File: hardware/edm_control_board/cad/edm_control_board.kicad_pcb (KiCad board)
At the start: 4 copper layers, 240 x 100 mm, 62 parts, among them J401 Conn_02x08_Odd_Even, J402 Conn_01x02, J403 Conn_01x02, J404 Conn_01x02, J405 Conn_01x06, Q201 BSS214NW, Q202 BSS214NW, Q203 BSS214NW, Q204 BSS214NW, SW501 SW_Push, SW502 SW_Push, SW503 SW_Push, SW504 SW_Push, U301 STM32F722RETx, U302 R-78E3.3-1.0, U303 L78L05_SO8, U501 NHD-0420H1Z, Y201 25M

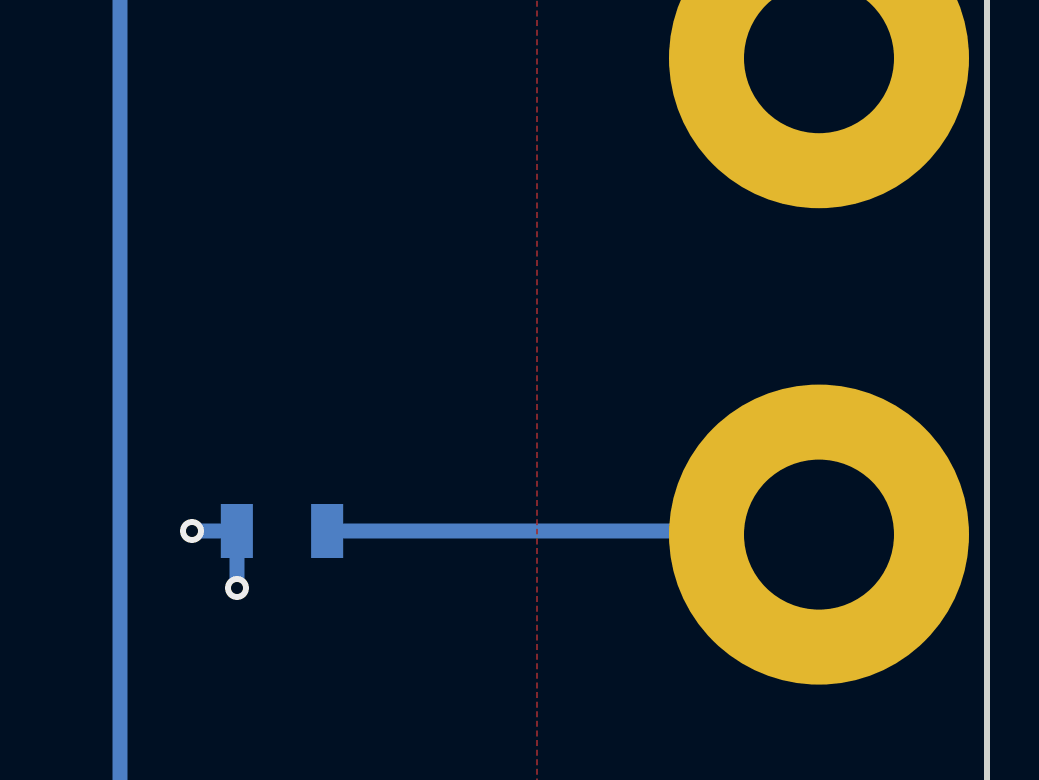
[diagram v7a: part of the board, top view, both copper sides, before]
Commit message: Add Y capacitor
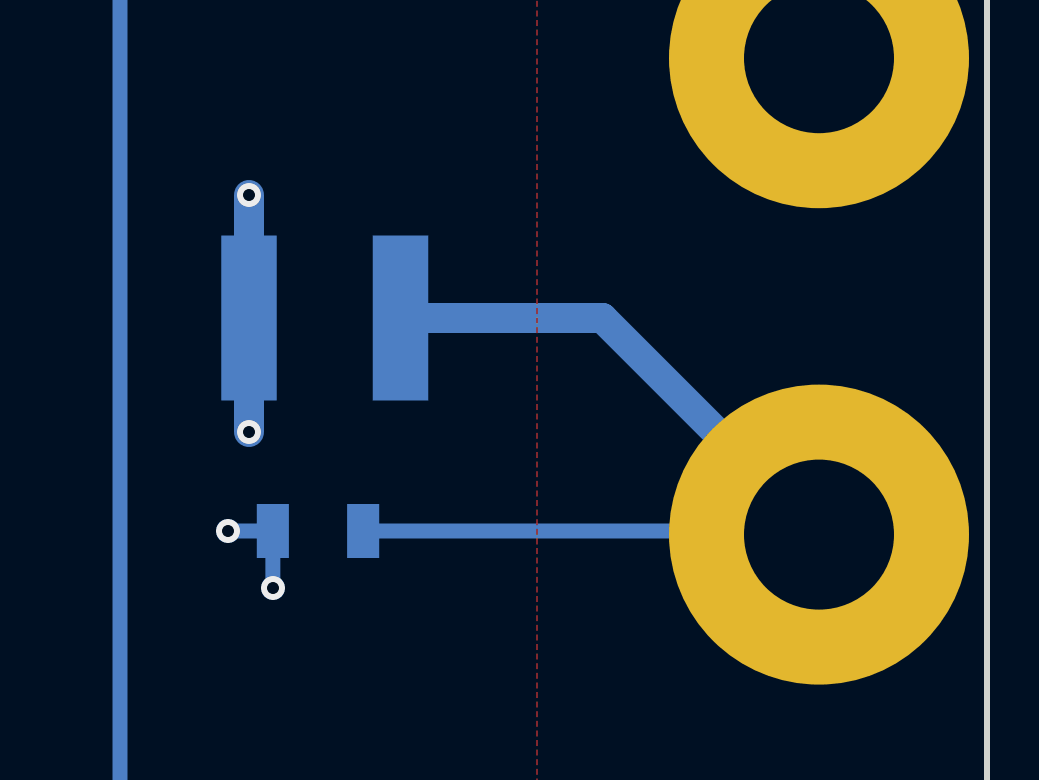
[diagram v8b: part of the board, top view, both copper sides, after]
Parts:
- added C401: 1800p, Capacitor_SMD:C_2220_5650Metric, B.Cu at (217.9, -33.4)
- moved R401 1.20 mm to (217.7, -26.3)
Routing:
- net /Connectors/Shield: track 16.4 -> 33.4 mm
- net GND: track 97.9 -> 105.8 mm, vias 27 -> 29
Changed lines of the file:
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@@
     (thickness 1.6)
     (drawings 34)
-    (tracks 490)
+    (tracks 496)
     (zones 0)
-    (modules 62)
+    (modules 63)
     (nets 68)
   )
@@
   )
   (setup
-    (last_trace_width 0.5)
+    (last_trace_width 1)
     (user_trace_width 0.25)
     (user_trace_width 0.5)
@@
     (uvia_drill 0.1)
   )
+  (module Capacitor_SMD:C_2220_5650Metric (layer B.Cu)
+    (at 217.925 -33.4 180)
+    (descr "Capacitor SMD 2220 (5650 Metric), square (rectangular) end terminal, IPC_7351 nominal, (Body size from: http://datasheets.avx.com/AVX-HV_MLCC.pdf), generated with kicad-footprint-generator")
+    (tags capacitor)
+    (attr smd)
+    (fp_text reference C401 (at 0 3.75 180) (layer B.SilkS)
+      (effects (font (size 1 1) (thickness 0.15)) (justify mirror))
+    )
+    (fp_text value 1800p (at 0 -3.75 180) (layer B.Fab)
+      (effects (font (size 1 1) (thickness 0.15)) (justify mirror))
+    )
+    (fp_line (start -2.85 -2.5) (end -2.85 2.5) (layer B.Fab) (width 0.1))
+    (fp_line (start -2.85 2.5) (end 2.85 2.5) (layer B.Fab) (width 0.1))
+    (fp_line (start 2.85 2.5) (end 2.85 -2.5) (layer B.Fab) (width 0.1))
+    (fp_line (start 2.85 -2.5) (end -2.85 -2.5) (layer B.Fab) (width 0.1))
+    (fp_line (start -1.28 2.61) (end 1.28 2.61) (layer B.SilkS) (width 0.12))
+    (fp_line (start -1.28 -2.61) (end 1.28 -2.61) (layer B.SilkS) (width 0.12))
+    (fp_line (start -3.7 -3) (end -3.7 3) (layer B.CrtYd) (width 0.05))
+    (fp_line (start -3.7 3) (end 3.7 3) (layer B.CrtYd) (width 0.05))
+    (fp_line (start 3.7 3) (end 3.7 -3) (layer B.CrtYd) (width 0.05))
+    (fp_line (start 3.7 -3) (end -3.7 -3) (layer B.CrtYd) (width 0.05))
+    (fp_text user %R (at 0 0 180) (layer B.Fab)
+      (effects (font (size 1 1) (thickness 0.15)) (justify mirror))
+    )
+    (pad 1 smd rect (at -2.525 0 180) (size 1.85 5.5) (layers B.Cu B.Paste B.Mask)
+      (net 63 /Connectors/Shield))
+    (pad 2 smd rect (at 2.525 0 180) (size 1.85 5.5) (layers B.Cu B.Paste B.Mask)
+      (net 12 GND))
+    (model ${KISYS3DMOD}/Capacitor_SMD.3dshapes/C_2220_5650Metric.wrl
+      (at (xyz 0 0 0))
+      (scale (xyz 1 1 1))
+      (rotate (xyz 0 0 0))
+    )
+  )
   (module Connector_PinHeader_2.54mm:PinHeader_2x08_P2.54mm_Vertical (layer B.Cu)
     (at 203 -39)
@@
   )
   (module Resistor_SMD:R_1206_3216Metric (layer B.Cu)
-    (at 216.5 -26.3 180)
+    (at 217.7 -26.3 180)
     (descr "Resistor SMD 1206 (3216 Metric), square (rectangular) end terminal, IPC_7351 nominal, (Body size source: http://www.tortai-tech.com/upload/download/2011102023233369053.pdf), generated with kicad-footprint-generator")
     (tags resistor)
@@
   (segment (start 165.5 -30) (end 165.5 -26.2) (width 0.5) (layer B.Cu) (net 11))
   (segment (start 179.38 -6.3) (end 182.08 -9) (width 0.5) (layer B.Cu) (net 11))
-  (segment (start 214.995 -26.3) (end 213.5 -26.3) (width 0.5) (layer B.Cu) (net 12))
-  (via (at 213.5 -26.3) (size 0.8) (drill 0.4) (layers F.Cu B.Cu) (net 12))
-  (segment (start 214.995 -24.405) (end 215 -24.4) (width 0.5) (layer B.Cu) (net 12))
-  (segment (start 214.995 -26.3) (end 214.995 -24.405) (width 0.5) (layer B.Cu) (net 12))
-  (via (at 215 -24.4) (size 0.8) (drill 0.4) (layers F.Cu B.Cu) (net 12))
+  (segment (start 215.4 -33.4) (end 215.4 -29.6) (width 1) (layer B.Cu) (net 12))
+  (via (at 215.4 -29.6) (size 0.8) (drill 0.4) (layers F.Cu B.Cu) (net 12))
+  (segment (start 215.4 -33.4) (end 215.4 -37.5) (width 1) (layer B.Cu) (net 12))
+  (via (at 215.4 -37.5) (size 0.8) (drill 0.4) (layers F.Cu B.Cu) (net 12))
+  (segment (start 216.195 -26.3) (end 214.7 -26.3) (width 0.5) (layer B.Cu) (net 12))
+  (via (at 214.7 -26.3) (size 0.8) (drill 0.4) (layers F.Cu B.Cu) (net 12))
+  (segment (start 216.195 -24.405) (end 216.2 -24.4) (width 0.5) (layer B.Cu) (net 12))
+  (segment (start 216.195 -26.3) (end 216.195 -24.405) (width 0.5) (layer B.Cu) (net 12))
+  (via (at 216.2 -24.4) (size 0.8) (drill 0.4) (layers F.Cu B.Cu) (net 12))
   (segment (start 201.6 -9) (end 197.6 -9) (width 2) (layer B.Cu) (net 12))
   (segment (start 206 -9) (end 201.6 -9) (width 2) (layer B.Cu) (net 12))
@@
   (segment (start 44.1 -22.6) (end 45.54999 -24.04999) (width 0.25) (layer B.Cu) (net 62))
   (segment (start 45.54999 -24.04999) (end 78.05001 -24.04999) (width 0.25) (layer B.Cu) (net 62))
-  (segment (start 218.005 -26.3) (end 234.28 -26.3) (width 0.5) (layer B.Cu) (net 63))
+  (segment (start 220.45 -33.4) (end 227.18 -33.4) (width 1) (layer B.Cu) (net 63))
+  (segment (start 227.18 -33.4) (end 234.4 -26.18) (width 1) (layer B.Cu) (net 63))
+  (segment (start 219.205 -26.3) (end 235.48 -26.3) (width 0.5) (layer B.Cu) (net 63))
   (segment (start 234.28 -26.3) (end 234.4 -26.18) (width 0.5) (layer B.Cu) (net 63))
   (segment (start 146.4136 -60.549989) (end 166.324979 -60.549989) (width 0.25) (layer F.Cu) (net 64))
